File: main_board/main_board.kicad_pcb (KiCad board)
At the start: 2 copper layers, 160 x 110 mm, 116 parts, among them IC1 MP2722GRH-0000-Z, IC2 MP3429GL-Z, IC3 NX3DV42GU, IC5 CY7C65632-28LTXC, J1 USB3_A, J10 Conn_01x22_Female, J2 USB3_A, J22 690-019-298-412, J3 Bus_M.2_Socket_M, J4 USB_B_Micro, J5 USB_C_Receptacle_USB2.0, J6 USB_A, J7 USB_A, U1 AP3441SHE-7B, U12 RT9742SNGV, U2 ASEK-32.768KHZ-L-R-T, U3 ATmega32U4-M, U4 AP22653W6, U6 AP22653W6, Y1 Crystal, Y2 Crystal

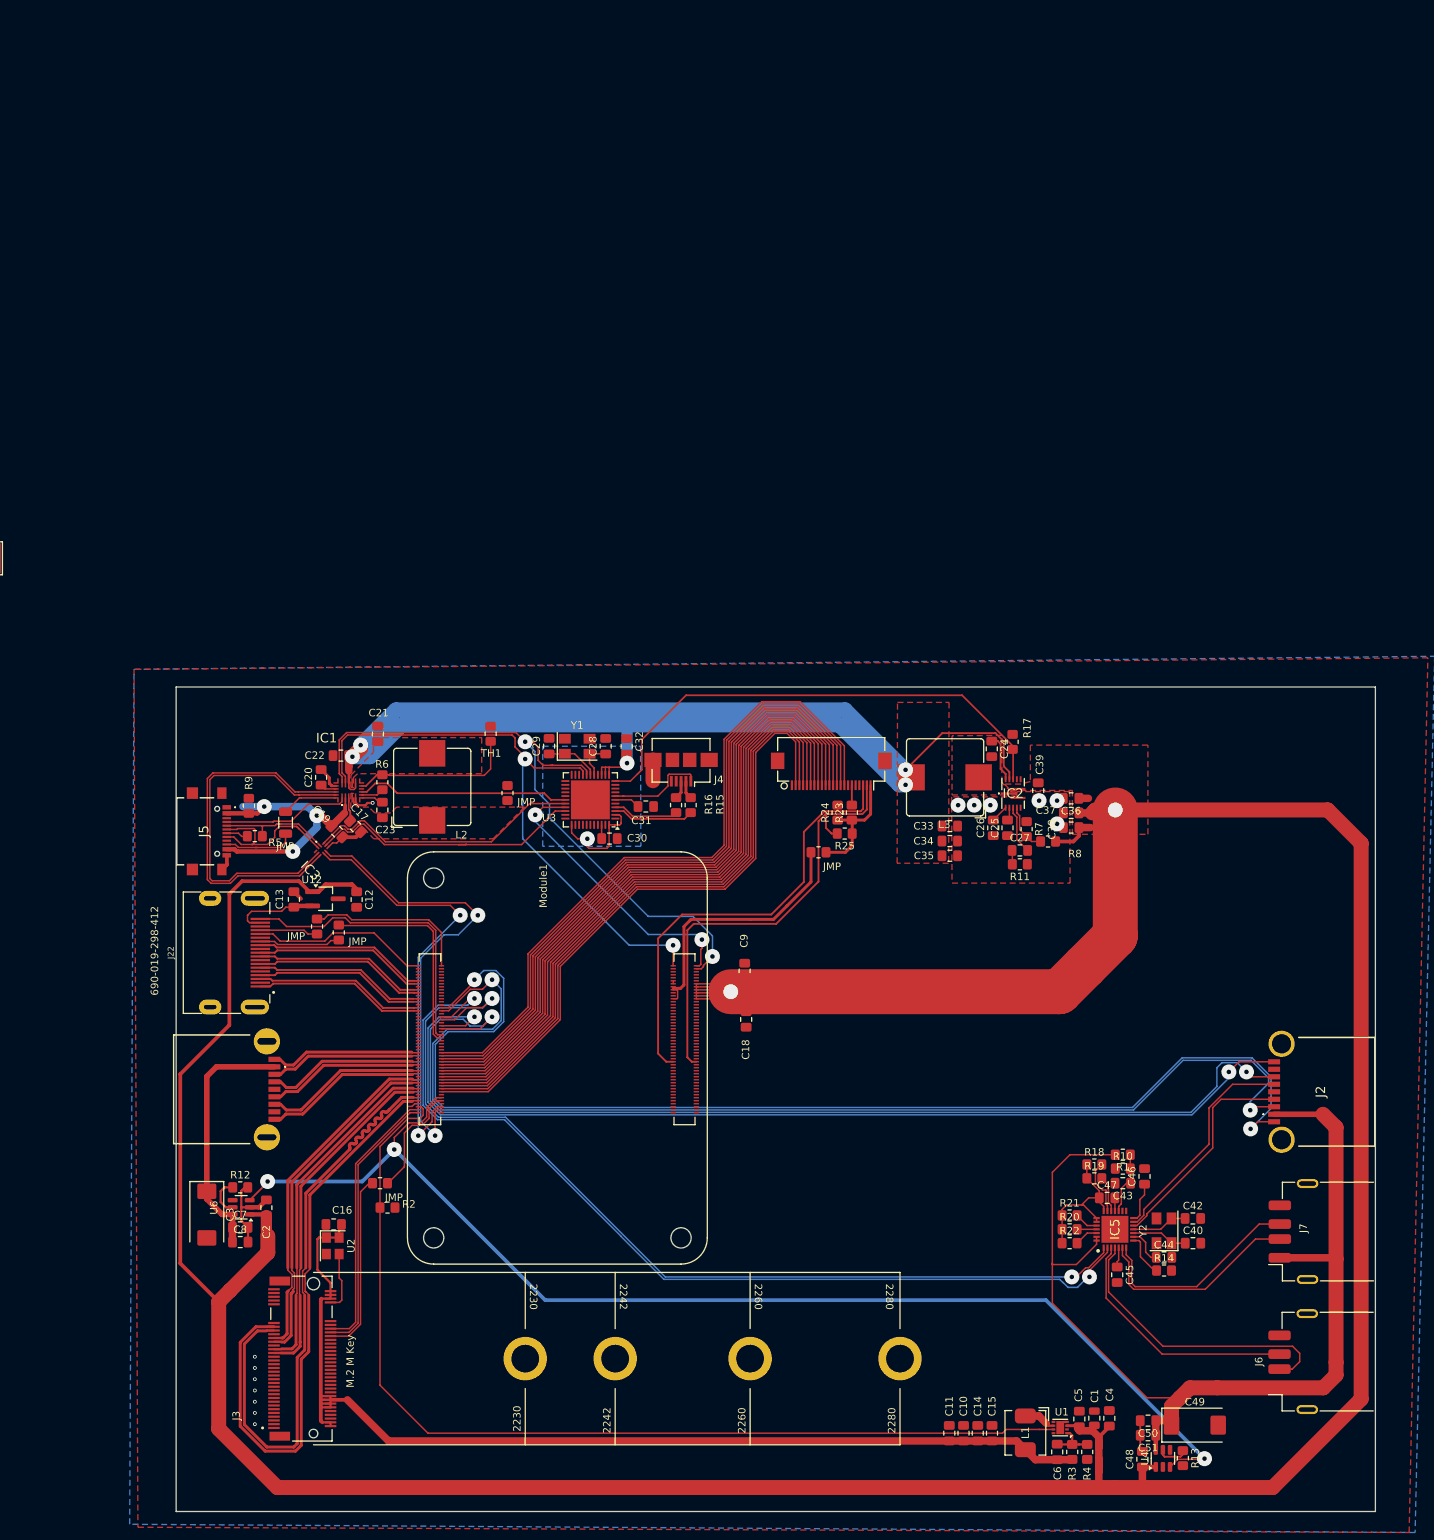
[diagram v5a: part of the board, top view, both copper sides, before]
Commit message: Bunch of fixes + audio out interface
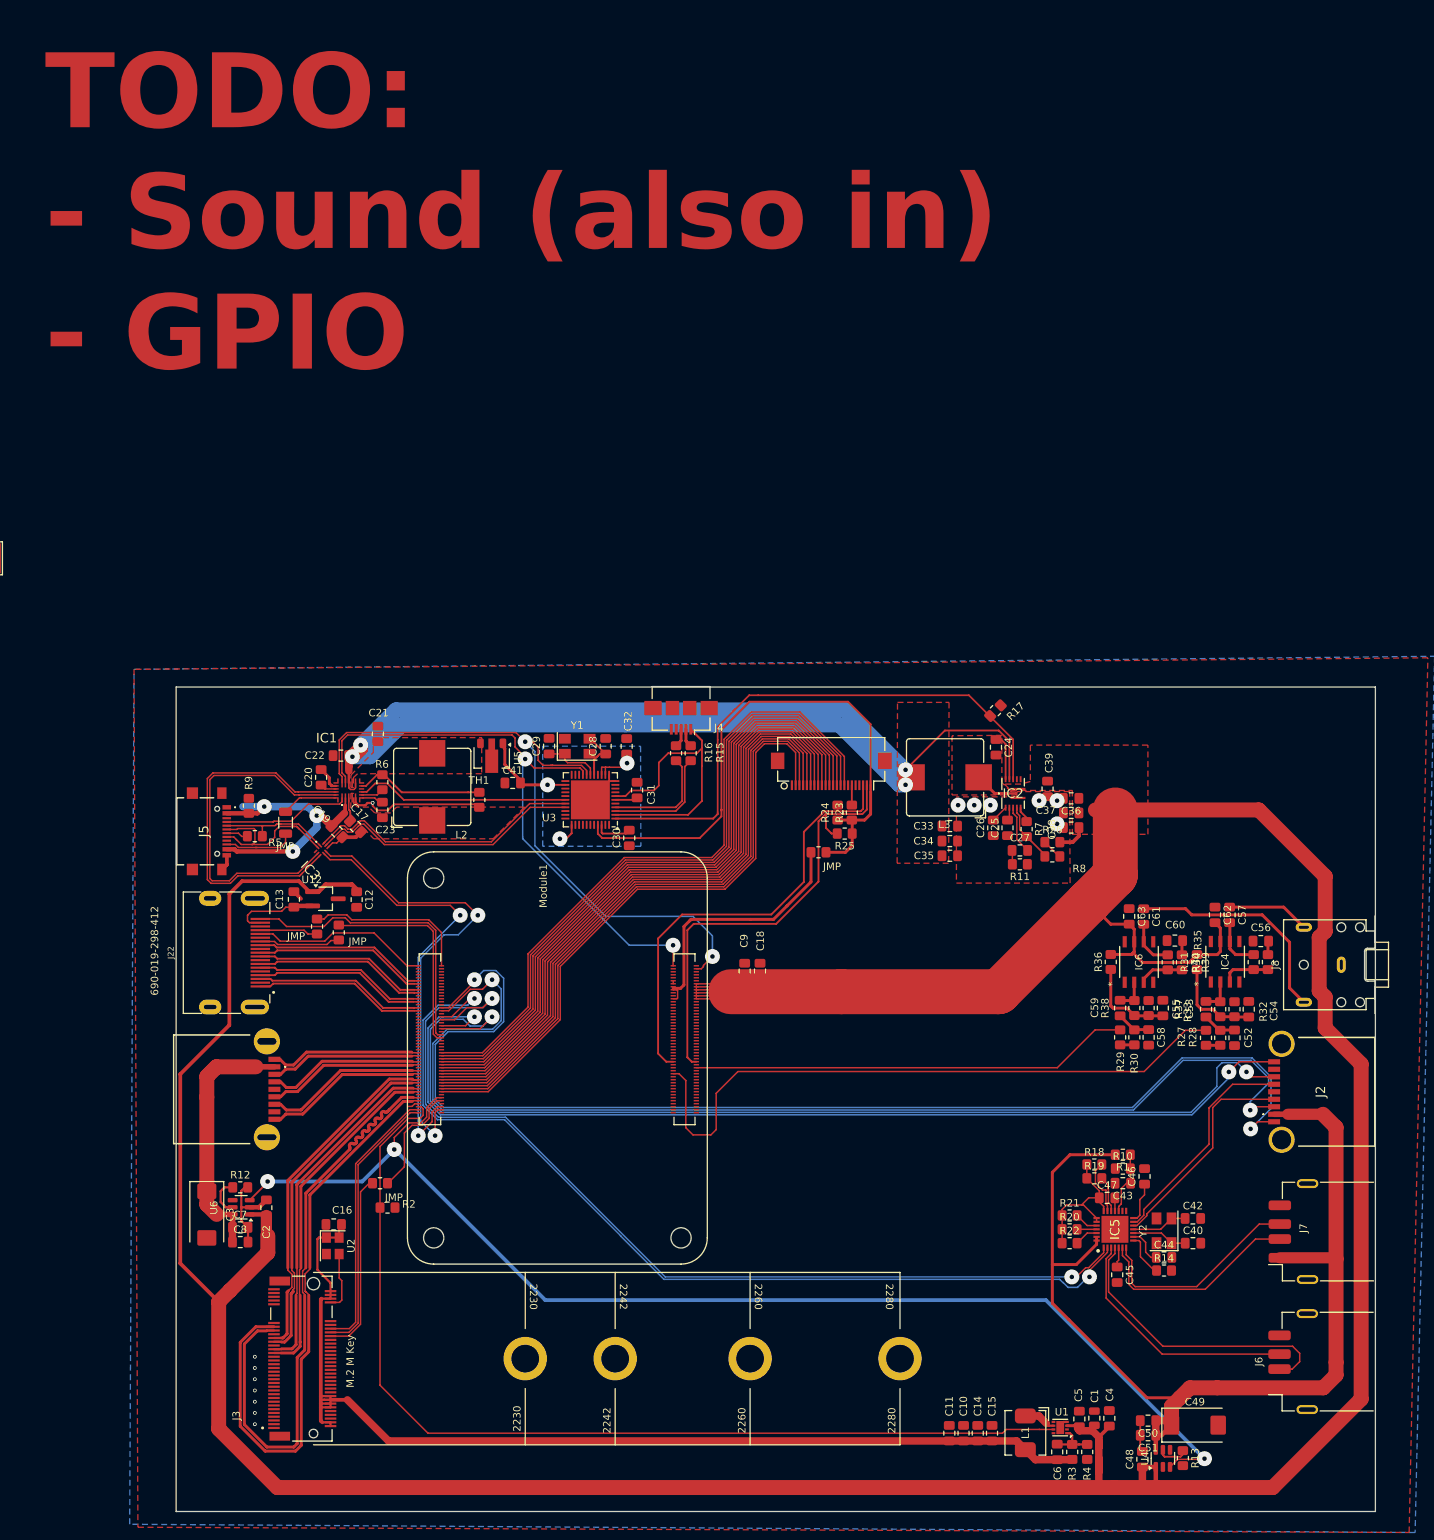
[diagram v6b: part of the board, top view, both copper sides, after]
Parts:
- removed the JMP at (72.1, 33.8)
- added C41: 100n, Capacitor_SMD:C_0805_2012Metric_Pad1.18x1.45mm_HandSolder, F.Cu at (72.8, 32.5)
- added C52: 1n, Capacitor_SMD:C_0805_2012Metric_Pad1.18x1.45mm_HandSolder, F.Cu at (169.1, 66.5)
- added C53: 1u, Capacitor_SMD:C_0805_2012Metric_Pad1.18x1.45mm_HandSolder, F.Cu at (159.5, 62.5)
- added C54: 1u, Capacitor_SMD:C_0805_2012Metric_Pad1.18x1.45mm_HandSolder, F.Cu at (171.0, 62.7)
- added C55: 100n, Capacitor_SMD:C_0805_2012Metric_Pad1.18x1.45mm_HandSolder, F.Cu at (165.3, 62.7)
- added C56: 10u, Capacitor_SMD:C_0805_2012Metric_Pad1.18x1.45mm_HandSolder, F.Cu at (172.6, 53.6)
- added C57: 10u, Capacitor_SMD:C_0805_2012Metric_Pad1.18x1.45mm_HandSolder, F.Cu at (168.4, 50.1)
- added C58: 1n, Capacitor_SMD:C_0805_2012Metric_Pad1.18x1.45mm_HandSolder, F.Cu at (157.6, 66.4)
- added C59: 100n, Capacitor_SMD:C_0805_2012Metric_Pad1.18x1.45mm_HandSolder, F.Cu at (153.8, 62.5)
- added C60: 10u, Capacitor_SMD:C_0805_2012Metric_Pad1.18x1.45mm_HandSolder, F.Cu at (161.1, 53.5)
- added C61: 10u, Capacitor_SMD:C_0805_2012Metric_Pad1.18x1.45mm_HandSolder, F.Cu at (157.0, 50.3)
- added C62: 10u, Capacitor_SMD:C_0805_2012Metric_Pad1.18x1.45mm_HandSolder, F.Cu at (166.5, 50.1)
- added C63: 10u, Capacitor_SMD:C_0805_2012Metric_Pad1.18x1.45mm_HandSolder, F.Cu at (155.1, 50.3)
- added IC4: TS921ID, 000_custom:S0-8_3P9X4P9_STM, F.Cu at (167.8, 56.4)
- added IC6: TS921ID, 000_custom:S0-8_3P9X4P9_STM, F.Cu at (156.4, 56.4)
- added J8: AudioJack3, Connector_Audio:Jack_3.5mm_CUI_SJ1-3523N_Horizontal, F.Cu at (183.3, 56.8)
- added R26: 430K, Resistor_SMD:R_0805_2012Metric_Pad1.20x1.40mm_HandSolder, F.Cu at (144.8, 40.4)
- added R27: 6K8, Resistor_SMD:R_0805_2012Metric_Pad1.20x1.40mm_HandSolder, F.Cu at (165.3, 66.5)
- added R28: 1K, Resistor_SMD:R_0805_2012Metric_Pad1.20x1.40mm_HandSolder, F.Cu at (167.2, 66.5)
- added R29: 6K8, Resistor_SMD:R_0805_2012Metric_Pad1.20x1.40mm_HandSolder, F.Cu at (153.8, 66.4)
- added R30: 1K, Resistor_SMD:R_0805_2012Metric_Pad1.20x1.40mm_HandSolder, F.Cu at (155.7, 66.4)
- added R31: 33K, Resistor_SMD:R_0805_2012Metric_Pad1.20x1.40mm_HandSolder, F.Cu at (164.1, 56.4)
- added R32: 33K, Resistor_SMD:R_0805_2012Metric_Pad1.20x1.40mm_HandSolder, F.Cu at (169.1, 62.7)
- added R33: 100k, Resistor_SMD:R_0805_2012Metric_Pad1.20x1.40mm_HandSolder, F.Cu at (167.2, 62.7)
- added R34: 10k, Resistor_SMD:R_0805_2012Metric_Pad1.20x1.40mm_HandSolder, F.Cu at (171.7, 56.4)
- added R35: 1k, Resistor_SMD:R_0805_2012Metric_Pad1.20x1.40mm_HandSolder, F.Cu at (173.6, 56.4)
- added R36: 33K, Resistor_SMD:R_0805_2012Metric_Pad1.20x1.40mm_HandSolder, F.Cu at (152.6, 56.4)
- added R37: 33K, Resistor_SMD:R_0805_2012Metric_Pad1.20x1.40mm_HandSolder, F.Cu at (157.6, 62.5)
- added R38: 100k, Resistor_SMD:R_0805_2012Metric_Pad1.20x1.40mm_HandSolder, F.Cu at (155.7, 62.5)
- added R39: 1k, Resistor_SMD:R_0805_2012Metric_Pad1.20x1.40mm_HandSolder, F.Cu at (162.1, 56.4)
- added R40: 10k, Resistor_SMD:R_0805_2012Metric_Pad1.20x1.40mm_HandSolder, F.Cu at (160.2, 56.4)
- added U5: AP2204RB-3.3, Package_TO_SOT_SMD:SOT-89-3, F.Cu at (70.0, 29.2)
- C20, C26: value 4.7u -> 10u
- C25: value 22n -> 100n
- C27: value 6.8n -> 10n
- C30: value 100n -> 1u
- L2: value L??? -> 4.7u
- R7: value Rfb1 -> 100K
- R8: value Rfb1 -> 33K
- moved TH1 8.94 mm to (68.3, 34.8), turned to -90 degrees
- moved J4 6.93 mm to (95.3, 23.8)
- moved R15 6.92 mm to (96.5, 28.5)
- moved R16 6.92 mm to (94.6, 28.5)
- moved C18 6.72 mm to (105.8, 57.6), turned to 90 degrees
- moved R17 4.76 mm to (137.2, 22.9), turned to -135 degrees
- moved C30 2.64 mm to (88.3, 39.8), turned to 90 degrees
- moved C31 2.48 mm to (89.4, 33.5), turned to -90 degrees
- moved R8 2.07 mm to (144.8, 42.3)
- moved C39 1.26 mm to (144.2, 33.3)
- moved C24 0.60 mm to (137.3, 27.7)
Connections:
- C32 pad 2: /Battery management/VBAT -> /Battery management/PMIC_3.3V
- IC2 pad 11: Net-(IC2-EN) -> /Battery management/BOOST_EN
- IC3 pad 9: /Battery management/USB_MUX_VCC -> /Battery management/USB_SW_VCC
- Module1 pad 28: /CM5_GPIO/GPIO13 -> /CM5_GPIO/AUDIO_OUT_L
- Module1 pad 31: /CM5_GPIO/GPIO12 -> /CM5_GPIO/AUDIO_OUT_R
- Module1 pad 93: unconnected-(Module1A-nRPIBOOT-Pad93) -> /CM5_GPIO/nRPIBOOT
- Module1 pad 99: /Battery management/CM5_PMIC_EN -> /CM5_GPIO/CM5_PMIC_EN
- R17 pad 2: Net-(IC2-EN) -> /Battery management/BOOST_EN
- R8 pad 2: /Battery management/+5V -> Net-(R26-Pad1)
- U3 pad 1: unconnected-(U3-PE6-Pad1) -> /Battery management/BOOST_EN
- U3 pad 11: Net-(IC2-EN) -> GND
- U3 pad 12: /Battery management/VBAT -> GND
- U3 pad 13: /Battery management/VBAT -> /Battery management/PMIC_3.3V
- U3 pad 14: /Battery management/VBAT -> /Battery management/PMIC_3.3V
- U3 pad 2: /Battery management/VBAT -> Net-(J4-VBUS)
- U3 pad 24: /Battery management/VBAT -> /Battery management/PMIC_3.3V
- U3 pad 30: /Battery management/CM5_PMIC_EN -> /Battery management/USB_SW_VCC
- U3 pad 31: /Battery management/USB_MUX_VCC -> unconnected-(U3-PC6-Pad31)
- U3 pad 34: /Battery management/VBAT -> /Battery management/PMIC_3.3V
- U3 pad 41: unconnected-(U3-PF0-Pad41) -> /CM5_GPIO/+3.3v
- U3 pad 44: /Battery management/VBAT -> /Battery management/PMIC_3.3V
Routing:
- net /CM5_GPIO/AUDIO_OUT_L: track 0.00 -> 86.8 mm
- net /Battery management/BOOST_EN: track 0.00 -> 74.9 mm
- net Net-(IC2-EN): track 66.9 -> 0.00 mm
- net /CM5_GPIO/+3.3v: track 51.6 -> 113.2 mm
- net /CM5_GPIO/AUDIO_OUT_R: track 0.00 -> 58.6 mm
- net /Battery management/CM5_PMIC_EN: track 38.1 -> 0.00 mm, vias 2 -> 0
- net /Battery management/USB_MUX_VCC: track 37.5 -> 0.00 mm
- net /Battery management/USB_SW_VCC: track 0.00 -> 36.7 mm
- net Net-(J4-VBUS): track 13.1 -> 44.1 mm
- net Net-(C61-Pad1): track 0.00 -> 30.1 mm
- net /Battery management/VBAT: track 212.7 -> 187.3 mm, vias 6 -> 4
- net /Battery management/PMIC_3.3V: track 0.00 -> 21.0 mm, vias 0 -> 3
- net /USB hub/VBUS: track 153.5 -> 174.4 mm
- net /Battery management/+5V: track 504.1 -> 523.1 mm, vias 2 -> 0
- net Net-(C53-Pad1): track 0.00 -> 12.4 mm
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- added copper zone on B.Cu, net /Battery management/PMIC_3.3V
- removed copper zone on B.Cu, net /Battery management/VBAT
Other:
- board text added: "TODO: - Sound (also in) - GPIO"
